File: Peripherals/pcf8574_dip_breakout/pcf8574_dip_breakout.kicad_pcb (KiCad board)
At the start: 2 copper layers, 28.6 x 25.4 mm, 26 parts, among them J1 I2C, J2 IO, U1 PCF8574

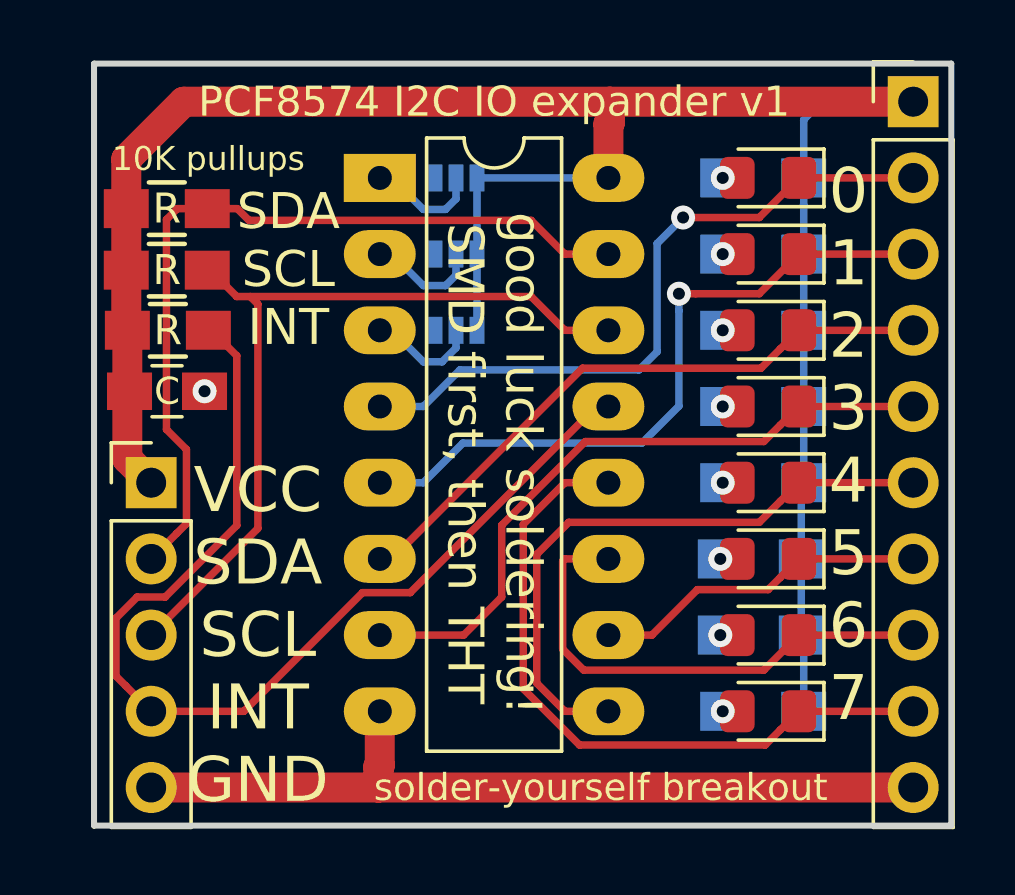
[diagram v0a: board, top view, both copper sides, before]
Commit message: Generating gerbers, adding some silk to the PCF8574 board
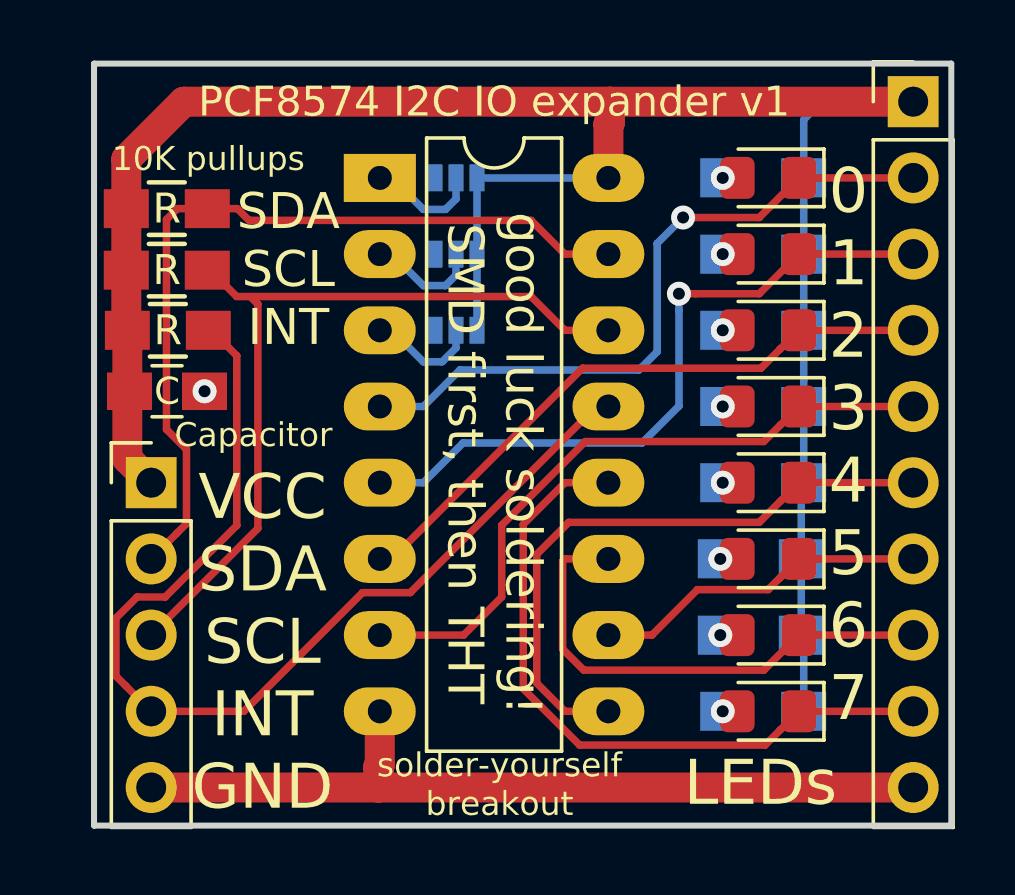
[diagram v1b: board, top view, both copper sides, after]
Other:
- board text added: "1K R"
- board text added: "Capacitor"
- board text added: "LEDs"
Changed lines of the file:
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@@
-(kicad_pcb (version 20171130) (host pcbnew 5.0.2-bee76a0~70~ubuntu18.04.1)
+(kicad_pcb (version 20171130) (host pcbnew "(5.1.2)-1")
   (general
     (thickness 1.6)
-    (drawings 13)
+    (drawings 16)
     (tracks 161)
     (zones 0)
@@
     (zone_45_only no)
     (trace_min 0.2)
-    (segment_width 0.2)
-    (edge_width 0.15)
     (via_size 0.8)
     (via_drill 0.4)
@@
     (uvia_min_size 0.2)
     (uvia_min_drill 0.1)
+    (edge_width 0.15)
+    (segment_width 0.2)
     (pcb_text_width 0.3)
     (pcb_text_size 1.5 1.5)
@@
     (solder_mask_min_width 0.25)
     (aux_axis_origin 168.91 39.37)
-    (visible_elements FFFFFF7F)
+    (visible_elements 7FFFFFFF)
     (pcbplotparams
-      (layerselection 0x010fc_ffffffff)
-      (usegerberextensions false)
+      (layerselection 0x010f0_ffffffff)
+      (usegerberextensions true)
       (usegerberattributes false)
       (usegerberadvancedattributes false)
@@
       (viasonmask false)
       (mode 1)
-      (useauxorigin false)
+      (useauxorigin true)
       (hpglpennumber 1)
       (hpglpenspeed 20)
@@
       (plotinvisibletext false)
       (padsonsilk false)
-      (subtractmaskfromsilk false)
+      (subtractmaskfromsilk true)
       (outputformat 1)
       (mirror false)
-      (drillshape 1)
+      (drillshape 0)
       (scaleselection 1)
-      (outputdirectory ""))
+      (outputdirectory "gerbers/"))
   )
   (net 0 "")
@@
       (net 12 GND))
   )
+  (gr_text Capacitor (at 145.65 51.75) (layer F.SilkS)
+    (effects (font (size 0.8 0.8) (thickness 0.15)))
+  )
+  (gr_text "1K R" (at 162.4 63.4) (layer B.SilkS)
+    (effects (font (size 1.5 1.5) (thickness 0.3)) (justify mirror))
+  )
+  (gr_text LEDs (at 162.55 63.35) (layer F.SilkS)
+    (effects (font (size 1.5 1.5) (thickness 0.3)))
+  )
   (gr_text "Ax jumpers need to be set" (at 153.543 40.64) (layer B.SilkS)
     (effects (font (size 1 1) (thickness 0.2)) (justify mirror))
@@
     (effects (font (size 1.5 1.5) (thickness 0.3)) (justify mirror))
   )
-  (gr_text "VCC\nSDA\nSCL\nINT\nGND" (at 145.796 58.42) (layer F.SilkS)
+  (gr_text "VCC\nSDA\nSCL\nINT\nGND" (at 145.95 58.65) (layer F.SilkS)
     (effects (font (size 1.5 1.5) (thickness 0.3)))
   )
@@
     (effects (font (size 1.2 1.2) (thickness 0.2)))
   )
-  (gr_text "solder-yourself breakout" (at 157.226 63.5) (layer F.SilkS)
-    (effects (font (size 0.9 0.9) (thickness 0.15)))
+  (gr_text "solder-yourself\nbreakout" (at 153.85 63.4) (layer F.SilkS)
+    (effects (font (size 0.8 0.8) (thickness 0.15)))
   )
   (gr_text "PCF8574 I2C IO expander v1" (at 153.67 40.64) (layer F.SilkS)

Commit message: Minor PCF8574 breakout changes
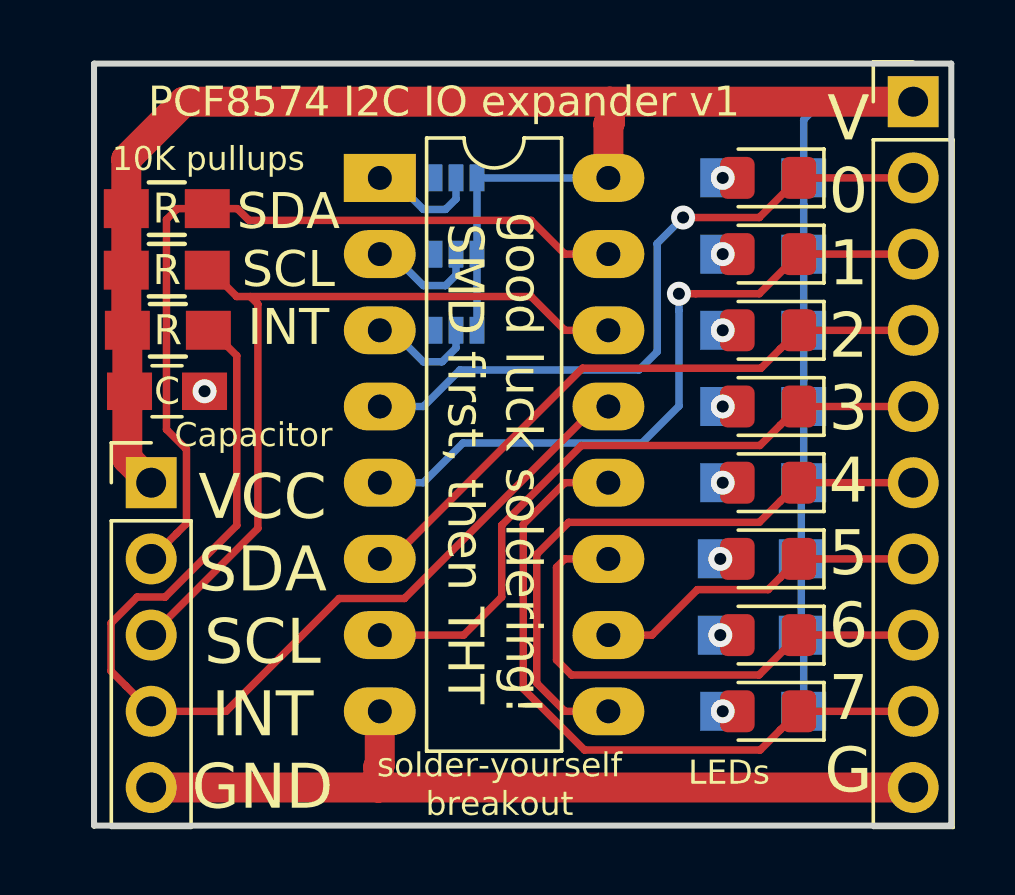
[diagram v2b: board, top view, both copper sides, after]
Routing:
- net /O6: track 16.9 -> 17.6 mm
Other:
- board text added: "V 0 1 2 3 4 5 6 7 G"
- board text removed: "0 1 2 3 4 5 6 7"
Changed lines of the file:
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@@
     (effects (font (size 0.8 0.8) (thickness 0.15)))
   )
-  (gr_text "1K R" (at 162.4 63.4) (layer B.SilkS)
-    (effects (font (size 1.5 1.5) (thickness 0.3)) (justify mirror))
+  (gr_text "1K R" (at 162.5 63) (layer B.SilkS)
+    (effects (font (size 0.8 0.8) (thickness 0.15)) (justify mirror))
   )
-  (gr_text LEDs (at 162.55 63.35) (layer F.SilkS)
-    (effects (font (size 1.5 1.5) (thickness 0.3)))
+  (gr_text LEDs (at 161.5 63) (layer F.SilkS)
+    (effects (font (size 0.8 0.8) (thickness 0.15)))
   )
   (gr_text "Ax jumpers need to be set" (at 153.543 40.64) (layer B.SilkS)
@@
     (effects (font (size 1.5 1.5) (thickness 0.3)))
   )
-  (gr_text "0\n1\n2\n3\n4\n5\n6\n7" (at 165.481 52.07) (layer F.SilkS)
+  (gr_text "V\n0\n1\n2\n3\n4\n5\n6\n7\nG" (at 165.481 52.07) (layer F.SilkS)
     (effects (font (size 1.5 1.5) (thickness 0.3)))
   )
@@
     (effects (font (size 0.8 0.8) (thickness 0.15)))
   )
-  (gr_text "PCF8574 I2C IO expander v1" (at 153.67 40.64) (layer F.SilkS)
+  (gr_text "PCF8574 I2C IO expander v1" (at 152 40.64) (layer F.SilkS)
     (effects (font (size 1 1) (thickness 0.2)))
   )
@@
   (via (at 161.29 45.72) (size 0.8) (drill 0.4) (layers F.Cu B.Cu) (net 7))
   (via (at 161.29 43.18) (size 0.8) (drill 0.4) (layers F.Cu B.Cu) (net 8))
-  (segment (start 149.283986 57.00501) (end 145.328996 60.96) (width 0.25) (layer F.Cu) (net 9))
-  (segment (start 145.328996 60.96) (end 142.24 60.96) (width 0.25) (layer F.Cu) (net 9))
-  (segment (start 150.87499 57.00501) (end 149.283986 57.00501) (width 0.25) (layer F.Cu) (net 9))
+  (segment (start 144.74 60.96) (end 142.24 60.96) (width 0.25) (layer F.Cu) (net 9))
+  (segment (start 148.5 57.2) (end 144.74 60.96) (width 0.25) (layer F.Cu) (net 9))
+  (segment (start 150.68 57.2) (end 148.5 57.2) (width 0.25) (layer F.Cu) (net 9))
   (segment (start 157.48 50.8) (end 157.08 50.8) (width 0.25) (layer F.Cu) (net 9))
-  (segment (start 157.08 50.8) (end 150.87499 57.00501) (width 0.25) (layer F.Cu) (net 9))
+  (segment (start 157.08 50.8) (end 150.68 57.2) (width 0.25) (layer F.Cu) (net 9))
+  (segment (start 141.390001 60.110001) (end 142.24 60.96) (width 0.25) (layer F.Cu) (net 9))
+  (segment (start 140.9 59.62) (end 141.390001 60.110001) (width 0.25) (layer F.Cu) (net 9))
+  (segment (start 140.9 58.020998) (end 140.9 59.62) (width 0.25) (layer F.Cu) (net 9))
+  (segment (start 144.245 48.26) (end 145.093001 49.108001) (width 0.25) (layer F.Cu) (net 9))
+  (segment (start 145.093001 49.108001) (end 145.093001 54.766001) (width 0.25) (layer F.Cu) (net 9))
   (segment (start 145.093001 54.766001) (end 142.709002 57.15) (width 0.25) (layer F.Cu) (net 9))
-  (segment (start 145.093001 49.108001) (end 145.093001 54.766001) (width 0.25) (layer F.Cu) (net 9))
+  (segment (start 142.709002 57.15) (end 141.770998 57.15) (width 0.25) (layer F.Cu) (net 9))
   (segment (start 144.145 48.26) (end 144.245 48.26) (width 0.25) (layer F.Cu) (net 9))
-  (segment (start 144.245 48.26) (end 145.093001 49.108001) (width 0.25) (layer F.Cu) (net 9))
-  (segment (start 141.390001 60.110001) (end 142.24 60.96) (width 0.25) (layer F.Cu) (net 9))
-  (segment (start 141.064999 59.784999) (end 141.390001 60.110001) (width 0.25) (layer F.Cu) (net 9))
-  (segment (start 141.064999 57.855999) (end 141.064999 59.784999) (width 0.25) (layer F.Cu) (net 9))
-  (segment (start 141.770998 57.15) (end 141.064999 57.855999) (width 0.25) (layer F.Cu) (net 9))
-  (segment (start 142.709002 57.15) (end 141.770998 57.15) (width 0.25) (layer F.Cu) (net 9))
+  (segment (start 141.770998 57.15) (end 140.9 58.020998) (width 0.25) (layer F.Cu) (net 9))
   (via (at 161.29 60.96) (size 0.8) (drill 0.4) (layers F.Cu B.Cu) (net 10))
   (segment (start 151.31 44.23) (end 150.26 43.18) (width 0.25) (layer B.Cu) (net 11))
@@
   (segment (start 157.48 58.42) (end 158.93 58.42) (width 0.25) (layer F.Cu) (net 16))
   (segment (start 167.64 58.42) (end 163.83 58.42) (width 0.25) (layer F.Cu) (net 17))
-  (segment (start 155.95499 58.885994) (end 156.657396 59.5884) (width 0.25) (layer F.Cu) (net 17))
-  (segment (start 155.95499 55.95501) (end 155.95499 58.885994) (width 0.25) (layer F.Cu) (net 17))
+  (segment (start 162.5 59.75) (end 163.83 58.42) (width 0.25) (layer F.Cu) (net 17))
+  (segment (start 156.25 59.75) (end 162.5 59.75) (width 0.25) (layer F.Cu) (net 17))
+  (segment (start 155.75 59.25) (end 156.25 59.75) (width 0.25) (layer F.Cu) (net 17))
+  (segment (start 155.75 56.16) (end 155.75 59.25) (width 0.25) (layer F.Cu) (net 17))
   (segment (start 157.48 55.88) (end 156.03 55.88) (width 0.25) (layer F.Cu) (net 17))
-  (segment (start 156.03 55.88) (end 155.95499 55.95501) (width 0.25) (layer F.Cu) (net 17))
-  (segment (start 162.6616 59.5884) (end 163.83 58.42) (width 0.25) (layer F.Cu) (net 17))
-  (segment (start 156.657396 59.5884) (end 162.6616 59.5884) (width 0.25) (layer F.Cu) (net 17))
+  (segment (start 156.03 55.88) (end 155.75 56.16) (width 0.25) (layer F.Cu) (net 17))
   (segment (start 167.64 43.18) (end 163.83 43.18) (width 0.25) (layer F.Cu) (net 18))
   (via (at 159.9692 44.5008) (size 0.8) (drill 0.4) (layers F.Cu B.Cu) (net 18))
@@
   (segment (start 151.31 50.8) (end 152.5292 49.5808) (width 0.25) (layer B.Cu) (net 18))
   (segment (start 163.83 60.96) (end 167.64 60.96) (width 0.25) (layer F.Cu) (net 19))
-  (segment (start 156.5186 62.08501) (end 162.70499 62.08501) (width 0.25) (layer F.Cu) (net 19))
-  (segment (start 154.642391 60.208801) (end 156.5186 62.08501) (width 0.25) (layer F.Cu) (net 19))
+  (segment (start 156.03 53.34) (end 154.64239 54.72761) (width 0.25) (layer F.Cu) (net 19))
+  (segment (start 157.48 53.34) (end 156.03 53.34) (width 0.25) (layer F.Cu) (net 19))
   (segment (start 154.64239 54.72761) (end 154.642391 60.208801) (width 0.25) (layer F.Cu) (net 19))
-  (segment (start 156.03 53.34) (end 154.64239 54.72761) (width 0.25) (layer F.Cu) (net 19))
+  (segment (start 154.642391 60.208801) (end 156.68359 62.25) (width 0.25) (layer F.Cu) (net 19))
   (segment (start 163.206628 61.583372) (end 163.83 60.96) (width 0.25) (layer F.Cu) (net 19))
-  (segment (start 162.70499 62.08501) (end 163.206628 61.583372) (width 0.25) (layer F.Cu) (net 19))
-  (segment (start 157.48 53.34) (end 156.03 53.34) (width 0.25) (layer F.Cu) (net 19))
+  (segment (start 156.68359 62.25) (end 162.54 62.25) (width 0.25) (layer F.Cu) (net 19))
+  (segment (start 162.54 62.25) (end 163.206628 61.583372) (width 0.25) (layer F.Cu) (net 19))
   (segment (start 163.83 45.72) (end 167.64 45.72) (width 0.25) (layer F.Cu) (net 20))
   (segment (start 162.5092 47.0408) (end 160.396295 47.0408) (width 0.25) (layer F.Cu) (net 20))
@@
   (segment (start 145.796 54.864) (end 145.796 47.38899) (width 0.25) (layer F.Cu) (net 22))
   (segment (start 163.83 50.8) (end 167.64 50.8) (width 0.25) (layer F.Cu) (net 23))
-  (segment (start 156.7116 51.9684) (end 162.6616 51.9684) (width 0.25) (layer F.Cu) (net 23))
   (segment (start 163.206628 51.423372) (end 163.83 50.8) (width 0.25) (layer F.Cu) (net 23))
-  (segment (start 162.6616 51.9684) (end 163.206628 51.423372) (width 0.25) (layer F.Cu) (net 23))
+  (segment (start 152.654 58.42) (end 153.924 57.15) (width 0.25) (layer F.Cu) (net 23))
   (segment (start 149.86 58.42) (end 152.654 58.42) (width 0.25) (layer F.Cu) (net 23))
   (segment (start 153.924 57.15) (end 153.924 54.756) (width 0.25) (layer F.Cu) (net 23))
-  (segment (start 152.654 58.42) (end 153.924 57.15) (width 0.25) (layer F.Cu) (net 23))
-  (segment (start 153.924 54.756) (end 156.7116 51.9684) (width 0.25) (layer F.Cu) (net 23))
+  (segment (start 153.924 54.756) (end 156.58 52.1) (width 0.25) (layer F.Cu) (net 23))
+  (segment (start 156.58 52.1) (end 162.53 52.1) (width 0.25) (layer F.Cu) (net 23))
+  (segment (start 162.53 52.1) (end 163.206628 51.423372) (width 0.25) (layer F.Cu) (net 23))
   (segment (start 156.03 45.72) (end 157.48 45.72) (width 0.25) (layer F.Cu) (net 24))
   (segment (start 154.90499 44.59499) (end 156.03 45.72) (width 0.25) (layer F.Cu) (net 24))
